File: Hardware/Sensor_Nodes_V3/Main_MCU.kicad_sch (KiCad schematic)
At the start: 21 parts, among them J6 Conn_01x27_Socket, J7 Conn_01x27_Socket, U1 STM32G474RBTx, U3 MCP2542FDxMF, U6 MCP2542FDxMF

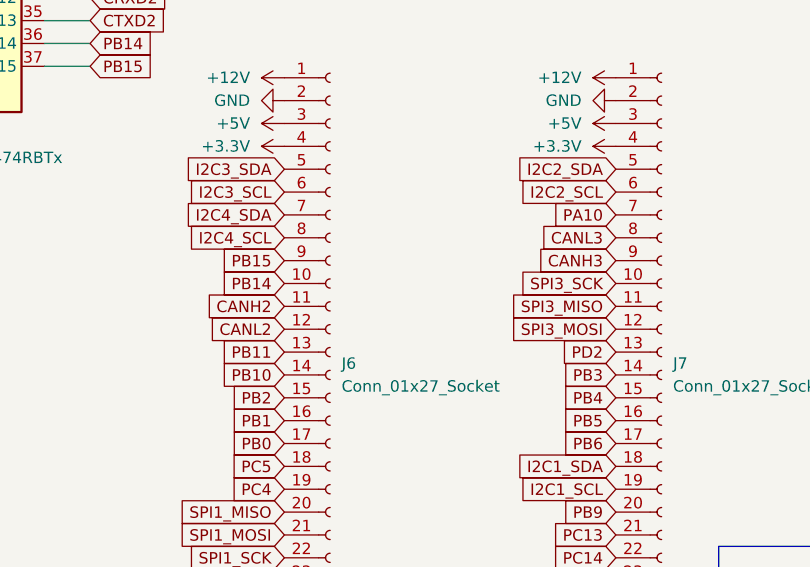
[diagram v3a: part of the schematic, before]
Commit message: DRC no error. GOOD. quick sync too.
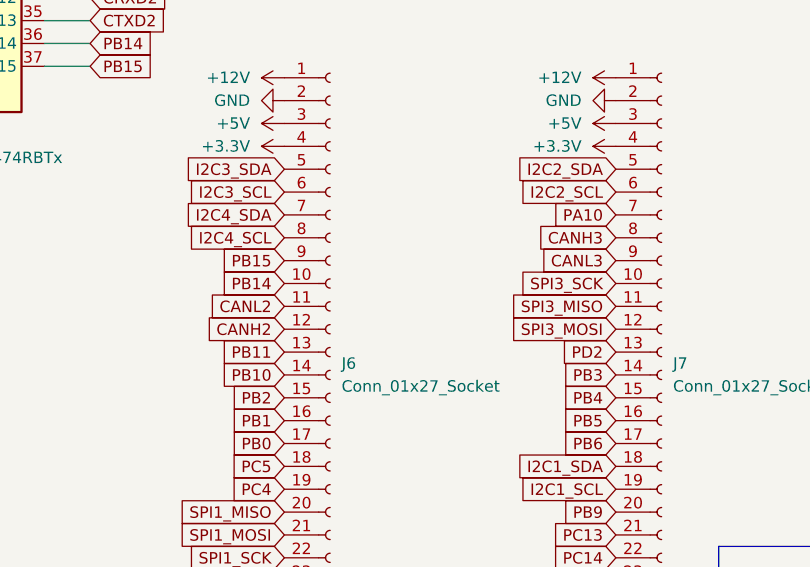
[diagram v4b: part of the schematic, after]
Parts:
- U3, U6: footprint Package_DFN_QFN:DFN-8-1EP_3x3mm_P0.65mm_EP1.55x2.4mm -> Package_SO:SOIC-8_3.9x4.9mm_P1.27mm
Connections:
- net CANH2: now also J6.12 (Pin_12); no longer J6.11 (Pin_11)
- net CANH3: now also J7.8 (Pin_8); no longer J7.9 (Pin_9)
- net CANL2: now also J6.11 (Pin_11); no longer J6.12 (Pin_12)
- net CANL3: now also J7.9 (Pin_9); no longer J7.8 (Pin_8)
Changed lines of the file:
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@@
 		)
 	)
+	(global_label "CANL2"
+		(shape input)
+		(at 95.25 139.7 180)
+		(fields_autoplaced yes)
+		(effects
+			(font
+				(size 1.27 1.27)
+			)
+			(justify right)
+		)
+		(property "Intersheetrefs" "${INTERSHEET_REFS}"
+			(at 86.3381 139.7 0)
+			(effects
+				(font
+					(size 1.27 1.27)
+				)
+				(justify right)
+				(hide yes)
+			)
+		)
+	)
 	(global_label "PC1"
 		(shape input)
@@
 		)
 	)
-	(global_label "CANH3"
-		(shape input)
-		(at 132.08 134.62 180)
-		(fields_autoplaced yes)
-		(effects
-			(font
-				(size 1.27 1.27)
-			)
-			(justify right)
-		)
-		(property "Intersheetrefs" "${INTERSHEET_REFS}"
-			(at 122.8657 134.62 0)
-			(effects
-				(font
-					(size 1.27 1.27)
-				)
-				(justify right)
-				(hide yes)
-			)
-		)
-	)
 	(global_label "T_RST"
 		(shape input)
@@
 		)
 	)
-	(global_label "CANH2"
+	(global_label "SPI3_SCK"
 		(shape input)
-		(at 95.25 139.7 180)
+		(at 27.94 80.01 180)
 		(fields_autoplaced yes)
 		(effects
@@
 		)
 		(property "Intersheetrefs" "${INTERSHEET_REFS}"
-			(at 86.0357 139.7 0)
+			(at 15.9439 80.01 0)
 			(effects
 				(font
@@
 		)
 	)
-	(global_label "SPI3_SCK"
+	(global_label "CANH2"
 		(shape input)
-		(at 27.94 80.01 180)
+		(at 95.25 142.24 180)
 		(fields_autoplaced yes)
 		(effects
@@
 		)
 		(property "Intersheetrefs" "${INTERSHEET_REFS}"
-			(at 15.9439 80.01 0)
+			(at 86.0357 142.24 0)
 			(effects
 				(font
@@
 		)
 	)
-	(global_label "CANL2"
-		(shape input)
-		(at 95.25 142.24 180)
-		(fields_autoplaced yes)
-		(effects
-			(font
-				(size 1.27 1.27)
-			)
-			(justify right)
-		)
-		(property "Intersheetrefs" "${INTERSHEET_REFS}"
-			(at 86.3381 142.24 0)
-			(effects
-				(font
-					(size 1.27 1.27)
-				)
-				(justify right)
-				(hide yes)
-			)
-		)
-	)
 	(global_label "SPI3_MOSI"
 		(shape input)
@@
 		)
 	)
+	(global_label "CANH3"
+		(shape input)
+		(at 132.08 132.08 180)
+		(fields_autoplaced yes)
+		(effects
+			(font
+				(size 1.27 1.27)
+			)
+			(justify right)
+		)
+		(property "Intersheetrefs" "${INTERSHEET_REFS}"
+			(at 122.8657 132.08 0)
+			(effects
+				(font
+					(size 1.27 1.27)
+				)
+				(justify right)
+				(hide yes)
+			)
+		)
+	)
 	(global_label "PC4"
 		(shape input)
@@
 		)
 	)
-	(global_label "CANL3"
-		(shape input)
-		(at 132.08 132.08 180)
-		(fields_autoplaced yes)
-		(effects
-			(font
-				(size 1.27 1.27)
-			)
-			(justify right)
-		)
-		(property "Intersheetrefs" "${INTERSHEET_REFS}"
-			(at 123.1681 132.08 0)
-			(effects
-				(font
-					(size 1.27 1.27)
-				)
-				(justify right)
-				(hide yes)
-			)
-		)
-	)
 	(global_label "PA4"
 		(shape input)
@@
 		)
 	)
+	(global_label "CANL3"
+		(shape input)
+		(at 132.08 134.62 180)
+		(fields_autoplaced yes)
+		(effects
+			(font
+				(size 1.27 1.27)
+			)
+			(justify right)
+		)
+		(property "Intersheetrefs" "${INTERSHEET_REFS}"
+			(at 123.1681 134.62 0)
+			(effects
+				(font
+					(size 1.27 1.27)
+				)
+				(justify right)
+				(hide yes)
+			)
+		)
+	)
 	(global_label "PB3"
 		(shape input)
@@
 			)
 		)
-		(property "Footprint" "Package_DFN_QFN:DFN-8-1EP_3x3mm_P0.65mm_EP1.55x2.4mm"
+		(property "Footprint" "Package_SO:SOIC-8_3.9x4.9mm_P1.27mm"
 			(at 214.63 160.02 0)
 			(effects
@@
 			)
 		)
-		(property "Footprint" "Package_DFN_QFN:DFN-8-1EP_3x3mm_P0.65mm_EP1.55x2.4mm"
+		(property "Footprint" "Package_SO:SOIC-8_3.9x4.9mm_P1.27mm"
 			(at 260.35 160.02 0)
 			(effects
